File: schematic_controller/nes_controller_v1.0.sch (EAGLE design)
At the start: 12 parts

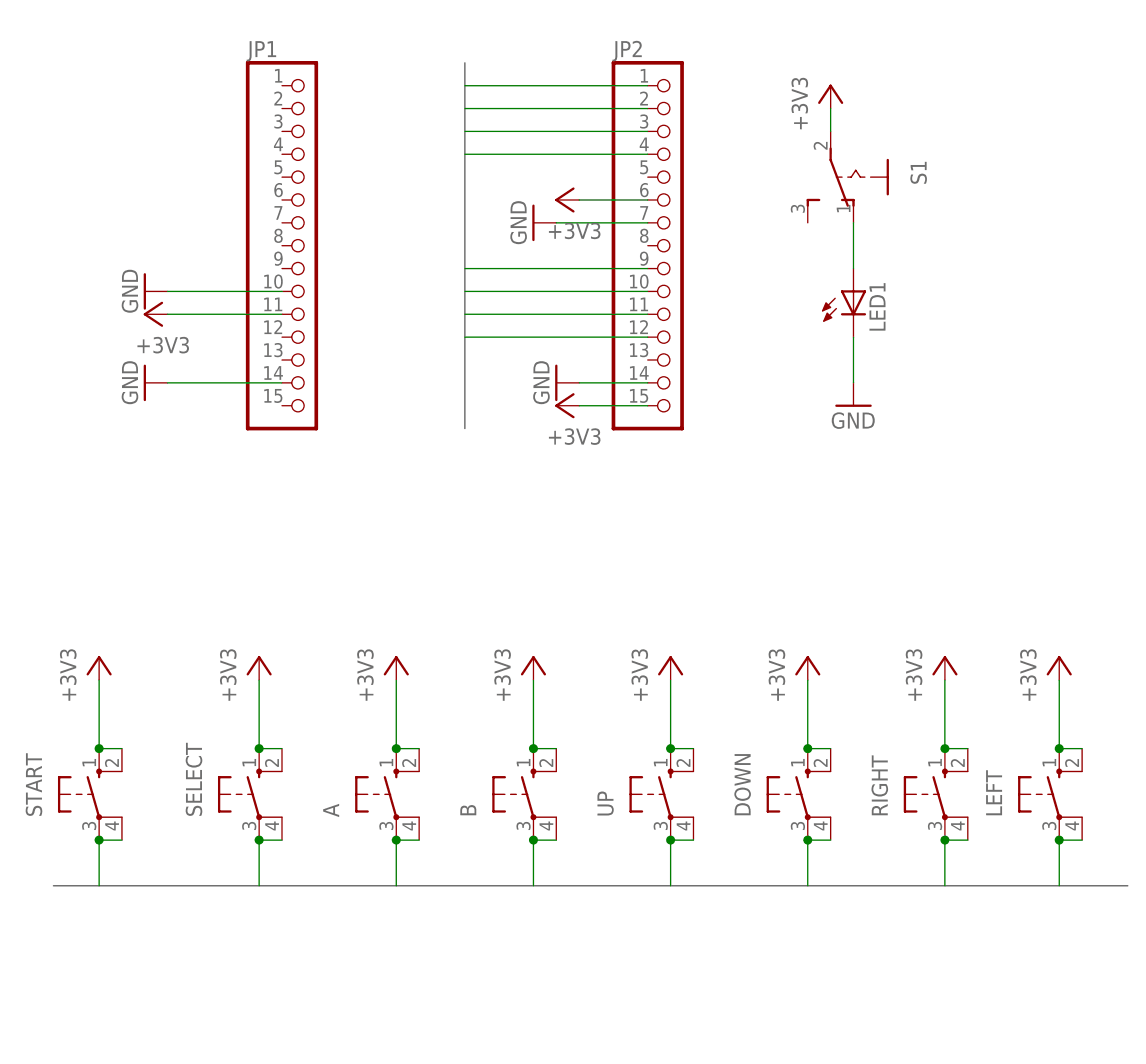
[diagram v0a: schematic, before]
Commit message: changed schematic
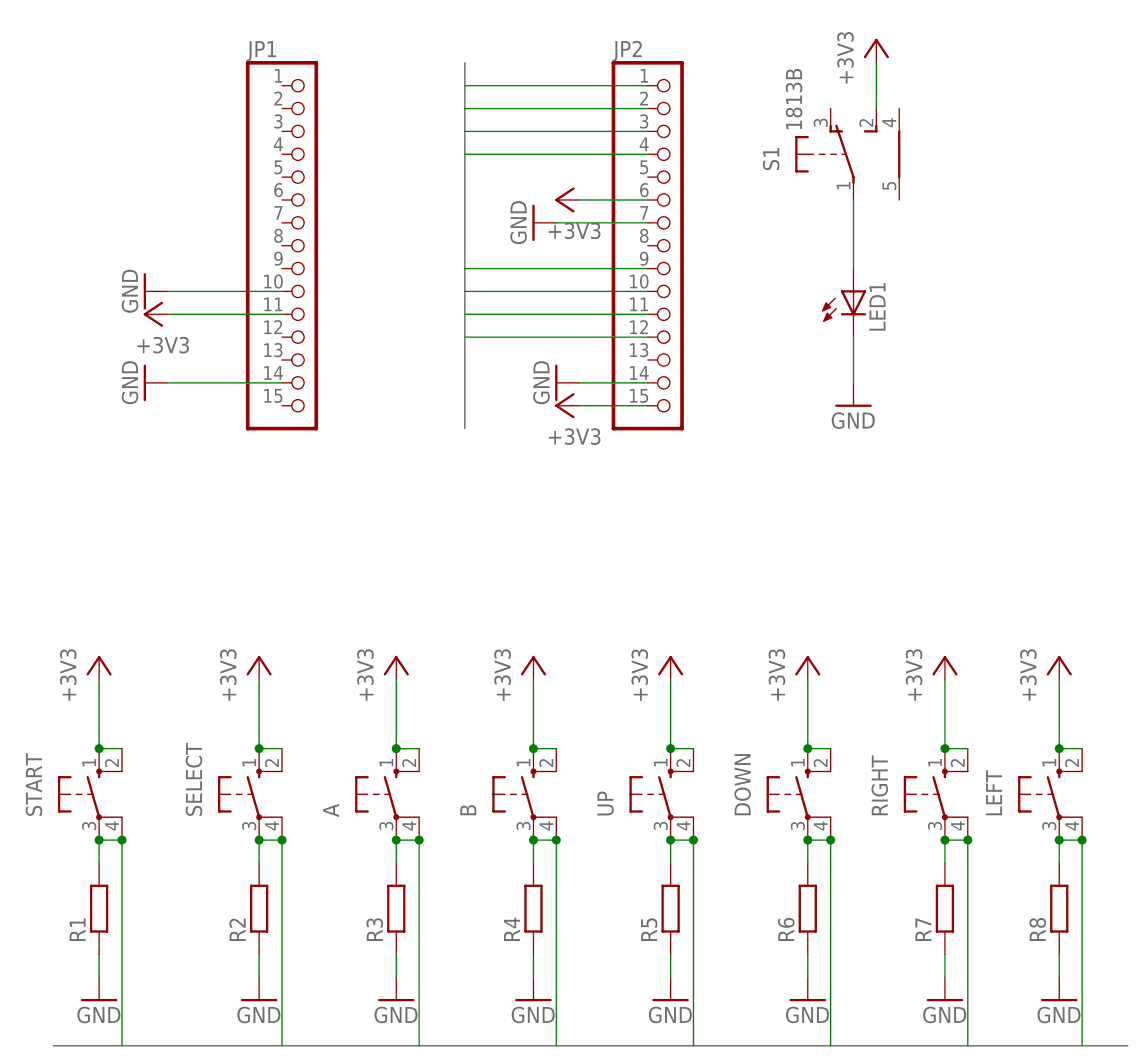
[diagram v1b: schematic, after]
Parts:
- added R1, R2, R3, R4, R5, R6, R7, R8: (no value), rcl:R-EU_MELF0207R
- S1: value (none) -> 1813B; device switch:M251 -> Benutzer_WM:1813B
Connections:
- net +3V3: now also S1.S; no longer S1.P
- net A: now also R3.2
- net B: now also R4.2
- net DOWN: now also R6.2
- net GND: now also R1.1, R2.1, R3.1, R4.1, R5.1, R6.1, R7.1, R8.1
- net LEFT: now also R8.2
- net N$1: now also S1.W; no longer S1.O
- net RIGHT: now also R7.2
- net SELECT: now also R2.2
- net START: now also R1.2
- net UP: now also R5.2
